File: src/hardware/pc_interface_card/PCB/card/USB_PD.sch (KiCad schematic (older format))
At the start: 34 parts, among them Q1 STL6P3LLH6, Q2 STL6P3LLH6, U4 STUSB4500QTR, U5 STUSB4500QTR

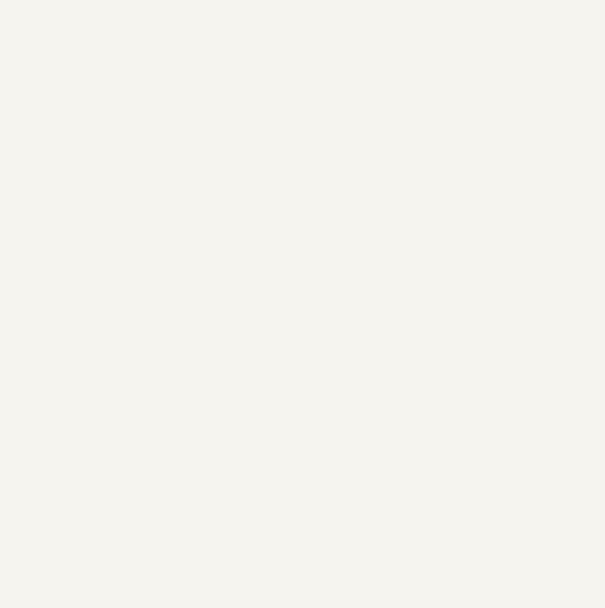
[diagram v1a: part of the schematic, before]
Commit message: adding barrel jack connector for powering PC interface card and mooving the status LEDs on the front panel
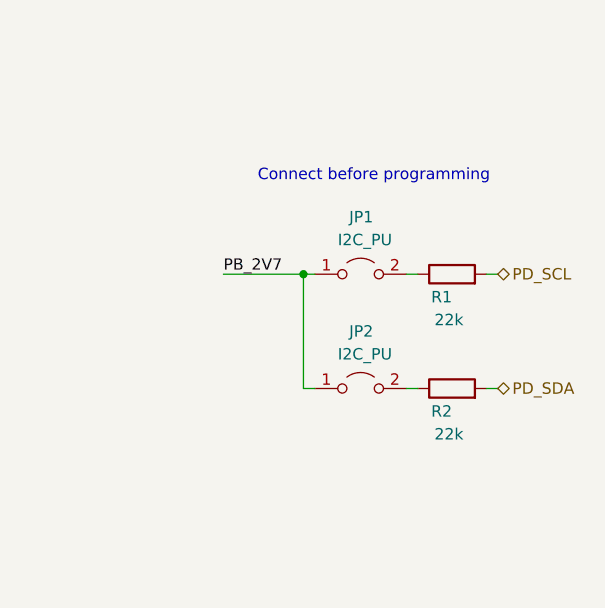
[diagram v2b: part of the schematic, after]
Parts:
- added JP1, JP2: I2C_PU, Connector_PinHeader_2.54mm:PinHeader_1x02_P2.54mm_Vertical, symbol Jumper:Jumper_2_Open
- added R1, R2: 22k, Resistor_SMD:R_0603_1608Metric, symbol Device:R
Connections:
- net PB_2V7: now also JP1.1 (A), JP2.1 (A)
- net PD_SCL: now also R1.2
- net PD_SDA: now also R2.2
- new net: JP1.2 (B), R1.1
- new net: JP2.2 (B), R2.1
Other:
- note added: "Connect before programming"
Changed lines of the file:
@@
 Text Label 1550 3100 0    50   ~ 0
 PB_2V7
+$Comp
+L Device:R R1
+U 1 1 5FB4E05C
+P 9100 5150
+F 0 "R1" V 9000 5150 50  0000 L CNN
+F 1 "22k" V 8900 5100 50  0000 L CNN
+F 2 "Resistor_SMD:R_0603_1608Metric" V 9030 5150 50  0001 C CNN
+F 3 "~" H 9100 5150 50  0001 C CNN
+	1    9100 5150
+	0    -1   -1   0
+$EndComp
+$Comp
+L Jumper:Jumper_2_Open JP1
+U 1 1 5FB573CD
+P 8700 5150
+F 0 "JP1" H 8650 5400 50  0000 L CNN
+F 1 "I2C_PU" H 8600 5300 50  0000 L CNN
+F 2 "Connector_PinHeader_2.54mm:PinHeader_1x02_P2.54mm_Vertical" H 8700 5150 50  0001 C CNN
+F 3 "~" H 8700 5150 50  0001 C CNN
+	1    8700 5150
+	1    0    0    -1
+$EndComp
+Wire Wire Line
+	8900 5150 8950 5150
+Text HLabel 9300 5150 2    50   BiDi ~ 0
+PD_SCL
+Wire Wire Line
+	9300 5150 9250 5150
+$Comp
+L Device:R R2
+U 1 1 5FB7949D
+P 9100 5650
+F 0 "R2" V 9000 5650 50  0000 L CNN
+F 1 "22k" V 8900 5600 50  0000 L CNN
+F 2 "Resistor_SMD:R_0603_1608Metric" V 9030 5650 50  0001 C CNN
+F 3 "~" H 9100 5650 50  0001 C CNN
+	1    9100 5650
+	0    -1   -1   0
+$EndComp
+$Comp
+L Jumper:Jumper_2_Open JP2
+U 1 1 5FB794A7
+P 8700 5650
+F 0 "JP2" H 8650 5900 50  0000 L CNN
+F 1 "I2C_PU" H 8600 5800 50  0000 L CNN
+F 2 "Connector_PinHeader_2.54mm:PinHeader_1x02_P2.54mm_Vertical" H 8700 5650 50  0001 C CNN
+F 3 "~" H 8700 5650 50  0001 C CNN
+	1    8700 5650
+	1    0    0    -1
+$EndComp
+Wire Wire Line
+	8900 5650 8950 5650
+Wire Wire Line
+	9300 5650 9250 5650
+Text HLabel 9300 5650 2    50   BiDi ~ 0
+PD_SDA
+Text Label 8100 5150 0    50   ~ 0
+PB_2V7
+Wire Wire Line
+	8100 5150 8450 5150
+Wire Wire Line
+	8450 5150 8450 5650
+Wire Wire Line
+	8450 5650 8500 5650
+Connection ~ 8450 5150
+Wire Wire Line
+	8450 5150 8500 5150
+Text Notes 8250 4750 0    50   ~ 0
+Connect before programming
 $EndSCHEMATC
